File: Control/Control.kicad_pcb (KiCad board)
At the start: 2 copper layers, 98 parts, among them J1 Conn_02x04_Odd_Even_Shielded, J2 Conn_01x03, J3 Conn_02x04_Odd_Even_Shielded, J4 Conn_01x03, J5 Conn_02x04_Odd_Even_Shielded, J6 Conn_02x04_Odd_Even_Shielded, J7 Conn_02x04_Odd_Even_Shielded, J8 Conn_02x04_Odd_Even_Shielded, SW1 SW_MEC_5E, SW2 SW_MEC_5E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

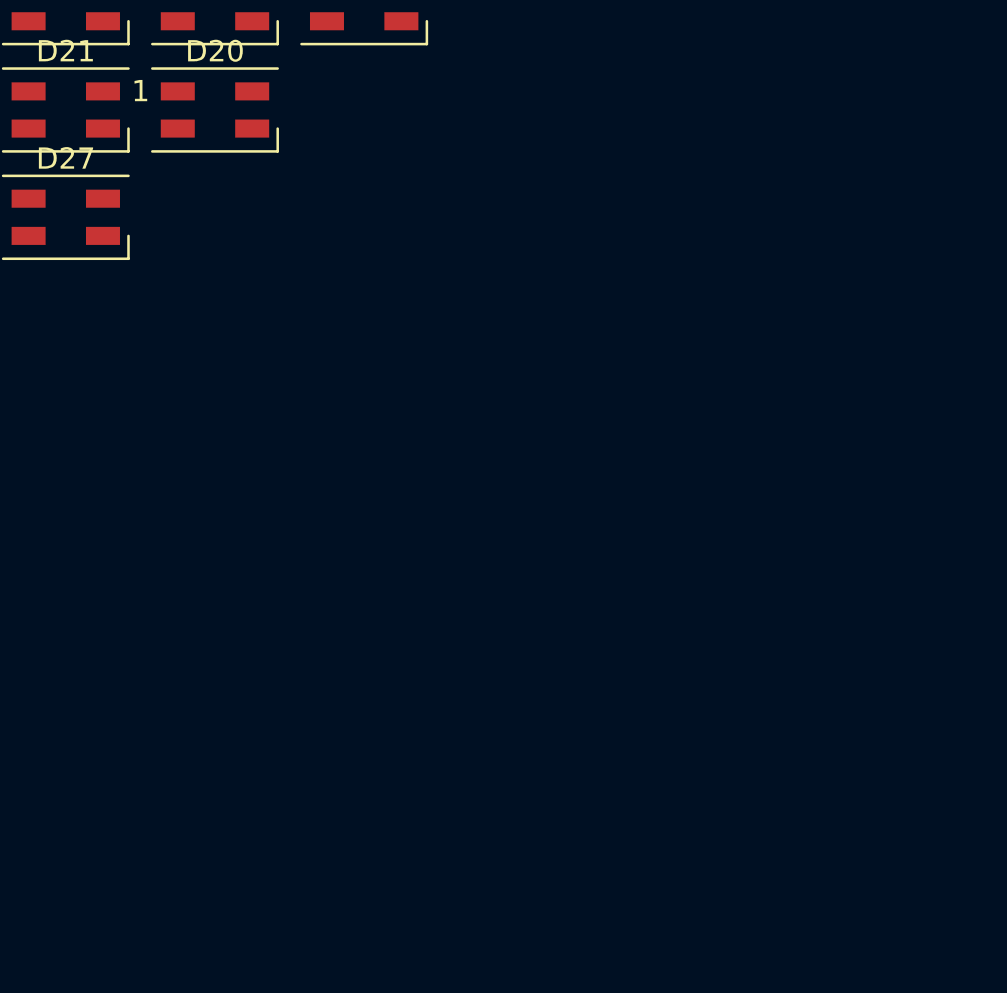
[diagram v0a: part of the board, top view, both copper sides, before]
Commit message: board config
will be resetting after finding a i2c oled on jlc
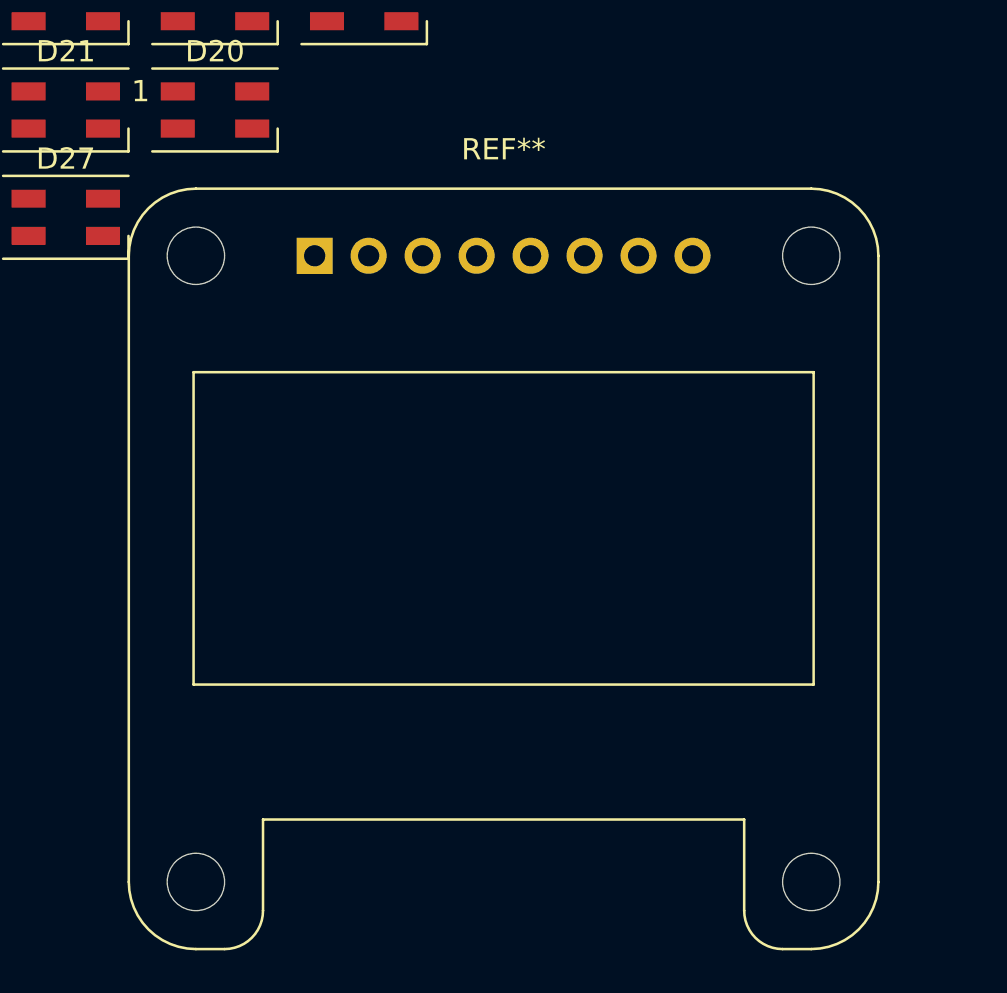
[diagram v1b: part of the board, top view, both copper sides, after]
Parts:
- added REF**: Adafruit_SSD1306, Display:Adafruit_SSD1306, F.Cu at (134.6, 91.4)
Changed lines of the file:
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@@
+    )
+  )
+  (footprint "Display:Adafruit_SSD1306" (layer "F.Cu")
+    (at 134.62 91.44)
+    (descr "Adafruit SSD1306 OLED 1.3 inch 128x64 I2C & SPI https://learn.adafruit.com/monochrome-oled-breakouts/downloads")
+    (tags "Adafruit SSD1306 OLED 1.3 inch 128x64 I2C & SPI ")
+    (attr through_hole)
+    (fp_text reference "REF**" (at 8.89 -5) (layer "F.SilkS")
+      (effects (font (size 1 1) (thickness 0.15)))
+    )
+    (fp_text value "Adafruit_SSD1306" (at 8.89 30) (layer "F.Fab")
+      (effects (font (size 1 1) (thickness 0.15)))
+    )
+    (fp_text user "${REFERENCE}" (at 8.89 14.732) (layer "F.Fab")
+      (effects (font (size 1 1) (thickness 0.15)))
+    )
+    (fp_line (start 23.368 -3.158) (end -5.588 -3.158) (layer "F.SilkS") (width 0.12))
+    (fp_line (start -5.698 20.176) (end 23.478 20.176) (layer "F.SilkS") (width 0.12))
+    (fp_line (start -2.43 26.526) (end -2.43 30.814) (layer "F.SilkS") (width 0.12))
+    (fp_line (start 20.21 26.526) (end 20.21 30.814) (layer "F.SilkS") (width 0.12))
+    (fp_line (start -5.698 5.478) (end -5.698 20.176) (layer "F.SilkS") (width 0.12))
+    (fp_line (start -5.698 5.478) (end 23.478 5.478) (layer "F.SilkS") (width 0.12))
+    (fp_line (start 22.018 32.622) (end 23.37 32.622) (layer "F.SilkS") (width 0.12))
+    (fp_line (start -4.238 32.622) (end -5.59 32.622) (layer "F.SilkS") (width 0.12))
+    (fp_line (start 23.478 5.478) (end 23.478 20.176) (layer "F.SilkS") (width 0.12))
+    (fp_line (start -8.746 0) (end -8.746 29.464) (layer "F.SilkS") (width 0.12))
+    (fp_line (start 26.526 0) (end 26.526 29.464) (layer "F.SilkS") (width 0.12))
+    (fp_line (start -2.43 26.526) (end 20.21 26.526) (layer "F.SilkS") (width 0.12))
+    (fp_arc (start -8.746 0) (mid -7.821043 -2.233043) (end -5.588 -3.158) (layer "F.SilkS") (width 0.12))
+    (fp_arc (start 23.368 -3.158) (mid 25.601043 -2.233043) (end 26.526 0) (layer "F.SilkS") (width 0.12))
+    (fp_arc (start -2.43 30.812) (mid -2.958137 32.091035) (end -4.236 32.622) (layer "F.SilkS") (width 0.12))
+    (fp_arc (start -5.588 32.622) (mid -7.821043 31.697043) (end -8.746 29.464) (layer "F.SilkS") (width 0.12))
+    (fp_arc (start 26.526 29.464) (mid 25.601043 31.697043) (end 23.368 32.622) (layer "F.SilkS") (width 0.12))
+    (fp_arc (start 22.016 32.622) (mid 20.738137 32.091035) (end 20.21 30.812) (layer "F.SilkS") (width 0.12))
+    (fp_line (start 26.67 0) (end 26.67 29.47) (layer "F.CrtYd") (width 0.05))
+    (fp_line (start 20.07 26.68) (end 20.07 30.82) (layer "F.CrtYd") (width 0.05))
+    (fp_line (start -8.89 0) (end -8.89 29.47) (layer "F.CrtYd") (width 0.05))
+    (fp_line (start 22.02 32.77) (end 23.37 32.77) (layer "F.CrtYd") (width 0.05))
+    (fp_line (start -2.29 26.68) (end -2.29 30.82) (layer "F.CrtYd") (width 0.05))
+    (fp_line (start -2.29 26.68) (end 20.07 26.68) (layer "F.CrtYd") (width 0.05))
+    (fp_line (start 23.37 -3.3) (end -5.59 -3.3) (layer "F.CrtYd") (width 0.05))
+    (fp_line (start -4.24 32.77) (end -5.59 32.77) (layer "F.CrtYd") (width 0.05))
+    (fp_arc (start -5.59 32.77) (mid -7.923452 31.803452) (end -8.89 29.47) (layer "F.CrtYd") (width 0.05))
+    (fp_arc (start 23.37 -3.3) (mid 25.703452 -2.333452) (end 26.67 0) (layer "F.CrtYd") (width 0.05))
+    (fp_arc (start 26.67 29.47) (mid 25.703452 31.803452) (end 23.37 32.77) (layer "F.CrtYd") (width 0.05))
+    (fp_arc (start 22.02 32.77) (mid 20.641142 32.198858) (end 20.07 30.82) (layer "F.CrtYd") (width 0.05))
+    (fp_arc (start -2.29 30.82) (mid -2.861142 32.198858) (end -4.24 32.77) (layer "F.CrtYd") (width 0.05))
+    (fp_arc (start -8.89 0) (mid -7.923452 -2.333452) (end -5.59 -3.3) (layer "F.CrtYd") (width 0.05))
+    (fp_line (start 22.018 32.512) (end 23.37 32.512) (layer "F.Fab") (width 0.1))
+    (fp_line (start 26.416 0) (end 26.416 29.464) (layer "F.Fab") (width 0.1))
+    (fp_line (start -8.636 0) (end -8.636 29.464) (layer "F.Fab") (width 0.1))
+    (fp_line (start 20.32 26.416) (end 20.32 30.814) (layer "F.Fab") (width 0.1))
+    (fp_line (start -2.54 26.416) (end -2.54 30.814) (layer "F.Fab") (width 0.1))
+    (fp_line (start 0 -2.268) (end 0.78 -3.048) (layer "F.Fab") (width 0.1))
+    (fp_line (start 23.368 5.588) (end 23.368 20.066) (layer "F.Fab") (width 0.1))
+    (fp_line (start -0.78 -3.048) (end 0 -2.268) (layer "F.Fab") (width 0.1))
+    (fp_line (start -4.238 32.512) (end -5.59 32.512) (layer "F.Fab") (width 0.1))
+    (fp_line (start -5.588 5.588) (end 23.368 5.588) (layer "F.Fab") (width 0.1))
+    (fp_line (start 23.368 -3.048) (end -5.588 -3.048) (layer "F.Fab") (width 0.1))
+    (fp_line (start -2.54 26.416) (end 20.32 26.416) (layer "F.Fab") (width 0.1))
+    (fp_line (start -5.588 20.066) (end 23.368 20.066) (layer "F.Fab") (width 0.1))
+    (fp_line (start -5.588 5.588) (end -5.588 20.066) (layer "F.Fab") (width 0.1))
+    (fp_arc (start -8.636 0.002) (mid -7.744676 -2.153847) (end -5.59 -3.048) (layer "F.Fab") (width 0.1))
+    (fp_arc (start -5.59 32.512) (mid -7.744676 31.617847) (end -8.636 29.462) (layer "F.Fab") (width 0.1))
+    (fp_arc (start 26.416 29.464) (mid 25.523261 31.619261) (end 23.368 32.512) (layer "F.Fab") (width 0.1))
+    (fp_arc (start -2.54 30.812) (mid -3.035918 32.013253) (end -4.236 32.512) (layer "F.Fab") (width 0.1))
+    (fp_arc (start 23.368 -3.048) (mid 25.523261 -2.155261) (end 26.416 0) (layer "F.Fab") (width 0.1))
+    (fp_arc (start 22.016 32.512) (mid 20.815918 32.013253) (end 20.32 30.812) (layer "F.Fab") (width 0.1))
+    (pad "" np_thru_hole circle (at 23.368 29.464) (size 2.7 2.7) (drill 2.7) (layers *.Cu *.Mask))
+    (pad "" np_thru_hole circle (at -5.588 0) (size 2.7 2.7) (drill 2.7) (layers *.Cu *.Mask))
+    (pad "" np_thru_hole circle (at 23.368 0) (size 2.7 2.7) (drill 2.7) (layers *.Cu *.Mask))
+    (pad "" np_thru_hole circle (at -5.588 29.464) (size 2.7 2.7) (drill 2.7) (layers *.Cu *.Mask))
+    (pad "1" thru_hole rect (at 0 0) (size 1.7 1.7) (drill 1) (layers *.Cu *.Mask))
+    (pad "2" thru_hole circle (at 2.54 0) (size 1.7 1.7) (drill 1) (layers *.Cu *.Mask))
+    (pad "3" thru_hole circle (at 5.08 0) (size 1.7 1.7) (drill 1) (layers *.Cu *.Mask))
+    (pad "4" thru_hole circle (at 7.62 0) (size 1.7 1.7) (drill 1) (layers *.Cu *.Mask))
+    (pad "5" thru_hole circle (at 10.16 0) (size 1.7 1.7) (drill 1) (layers *.Cu *.Mask))
+    (pad "6" thru_hole circle (at 12.7 0) (size 1.7 1.7) (drill 1) (layers *.Cu *.Mask))
+    (pad "7" thru_hole circle (at 15.24 0) (size 1.7 1.7) (drill 1) (layers *.Cu *.Mask))
+    (pad "8" thru_hole circle (at 17.78 0) (size 1.7 1.7) (drill 1) (layers *.Cu *.Mask))
+    (model "${KICAD6_3DMODEL_DIR}/Display.3dshapes/Adafruit_SSD1306.wrl"
+      (offset (xyz 0 0 0))
+      (scale (xyz 1 1 1))
+      (rotate (xyz 0 0 0))
     )
   )

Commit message: cntrl gerber
easy eda routing
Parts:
- removed REF**: Adafruit_SSD1306, Display:Adafruit_SSD1306
- added C1: 0.1uF cap, Capacitor_THT:C_Disc_D4.3mm_W1.9mm_P5.00mm, F.Cu at (208.3, 137.2)
- added C2: 4.7uF cap, Capacitor_THT:C_Disc_D4.3mm_W1.9mm_P5.00mm, F.Cu at (221.0, 111.8)
- added C3: 4.7uF/16v, Capacitor_THT:C_Disc_D4.3mm_W1.9mm_P5.00mm, F.Cu at (239.3, 130.3)
- added C4: 0.1uF cap, Capacitor_THT:C_Disc_D4.3mm_W1.9mm_P5.00mm, F.Cu at (221.3, 131.5)
- added C5: 4.7uF/16v, Capacitor_THT:C_Disc_D4.3mm_W1.9mm_P5.00mm, F.Cu at (218.4, 137.2)
- added DS1: OLED-128O064D, Display:OLED-128O064D, F.Cu at (228.6, 104.1)
- added R43: 2.2k, Resistor_THT:R_Box_L8.4mm_W2.5mm_P5.08mm, F.Cu at (231.1, 144.8)
- added R44: 2.2k, Resistor_THT:R_Box_L8.4mm_W2.5mm_P5.08mm, F.Cu at (218.4, 119.4)
- added R45: 560k, Resistor_THT:R_Box_L8.4mm_W2.5mm_P5.08mm, F.Cu at (238.8, 118.0)
- moved R5 181.5 mm to (192.6, 130.4), turned to 90 degrees
- moved SW4 178.1 mm to (231.1, 85.0), turned to -90 degrees
- moved SW1 170.5 mm to (241.5, 76.2), turned to -90 degrees
- moved J8 161.0 mm to (189.1, 98.2), turned to 90 degrees
- moved SW5 159.6 mm to (220.8, 76.2), turned to -90 degrees
- moved R6 151.4 mm to (192.6, 153.4), turned to 90 degrees
- moved D40 138.5 mm to (55.2, 99.8), turned to -90 degrees
- moved R2 135.2 mm to (192.6, 61.4), turned to 90 degrees
- moved R36 133.9 mm to (67.6, 153.4), turned to 90 degrees
- moved R11 133.1 mm to (167.6, 130.4), turned to 90 degrees
- moved R9 131.9 mm to (167.6, 84.4), turned to 90 degrees
- moved R1 131.2 mm to (192.6, 38.4), turned to 90 degrees
- moved R30 129.1 mm to (92.6, 153.4), turned to 90 degrees
- moved R16 129.1 mm to (142.6, 107.4), turned to 90 degrees
- moved D37 128.1 mm to (55.2, 30.8), turned to -90 degrees
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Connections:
- D11 pad 1: Net-(D11-Pad1) -> (no net)
- D11 pad 2: GROUND -> (no net)
- D11 pad 3: 5VDC -> (no net)
- D11 pad 4: Net-(D11-Pad4) -> (no net)
- D2 pad 1: Net-(D2-Pad1) -> (no net)
- D2 pad 2: GROUND -> (no net)
- D2 pad 3: 5VDC -> (no net)
- D2 pad 4: Net-(D2-Pad4) -> (no net)
- D6 pad 1: unconnected-(D6-Pad1) -> (no net)
- D6 pad 2: GROUND -> (no net)
- D6 pad 3: 5VDC -> (no net)
- D6 pad 4: Net-(D12-Pad1) -> (no net)
- D7 pad 1: Net-(D13-Pad4) -> (no net)
- D7 pad 2: GROUND -> (no net)
- D7 pad 3: 5VDC -> (no net)
- D7 pad 4: Net-(D1-Pad1) -> (no net)
- D8 pad 1: Net-(D14-Pad4) -> (no net)
- D8 pad 2: GROUND -> (no net)
- D8 pad 3: 5VDC -> (no net)
- D8 pad 4: Net-(D2-Pad1) -> (no net)
- D9 pad 1: Net-(D15-Pad4) -> (no net)
- D9 pad 2: GROUND -> (no net)
- D9 pad 3: 5VDC -> (no net)
- D9 pad 4: Net-(D3-Pad1) -> (no net)
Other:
- board outline added: 213.4 x 137.2 mm
